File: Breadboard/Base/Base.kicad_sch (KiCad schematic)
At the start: 41 parts, among them J1 Barrel_Jack_Switch, J2 AudioJack2_Ground, J3 AudioJack2_Ground, J4 Conn_01x04_Pin, J5 Conn_01x04_Pin, J6 Conn_Coaxial, J7 Conn_Coaxial, J8 Conn_01x02_Pin, J9 Conn_01x02_Pin, Q1 40V, U1 TLE2426xD, U2 OPA1656

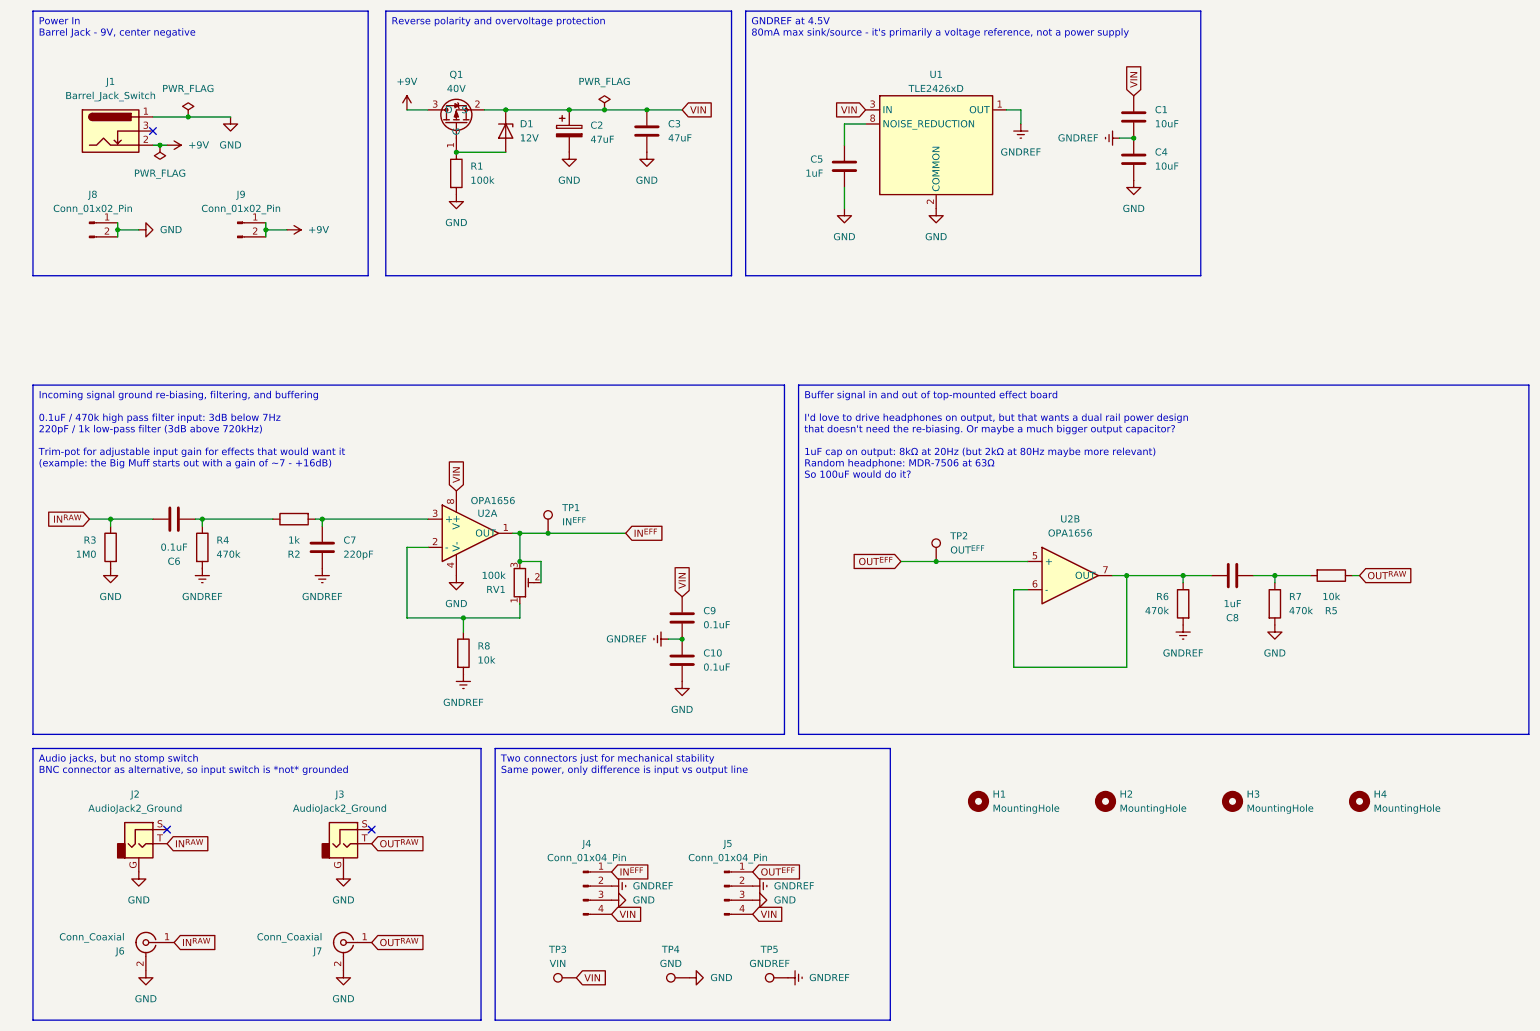
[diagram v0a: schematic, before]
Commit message: Stop trying to pretend that the 4.5V reference voltage is ground
Yes, it was a real ground in the earlier dual rail supply designs, but
in Gen2 that's no longer the case, and the pretense caused issues with
me adding bypass capacitors to that reference voltage rail.

So this just renames it as 'GNDREF' everywhere.  Maybe I should have
called it 'VREF'?

The real ground is still called '-V' in the effects, I'll change that
later too, but let's do this in individual steps.

This also removes the remaining bypass caps to GNDREF, and makes the
ground pours be actual ground.

I also need to come up with something sane for the Rectifier board
potentiometers.

Right now they are bogus random stuff where I am using the pots as
trim-pots for testing, but they don't actually make *sense* (ie the
"Volume" pot isn't actually sane, it ends up being another voltage
divider with the resistors in the low-pass filter trim pot etc).

Signed-off-by: Linus Torvalds <torvalds@linux-foundation.org>
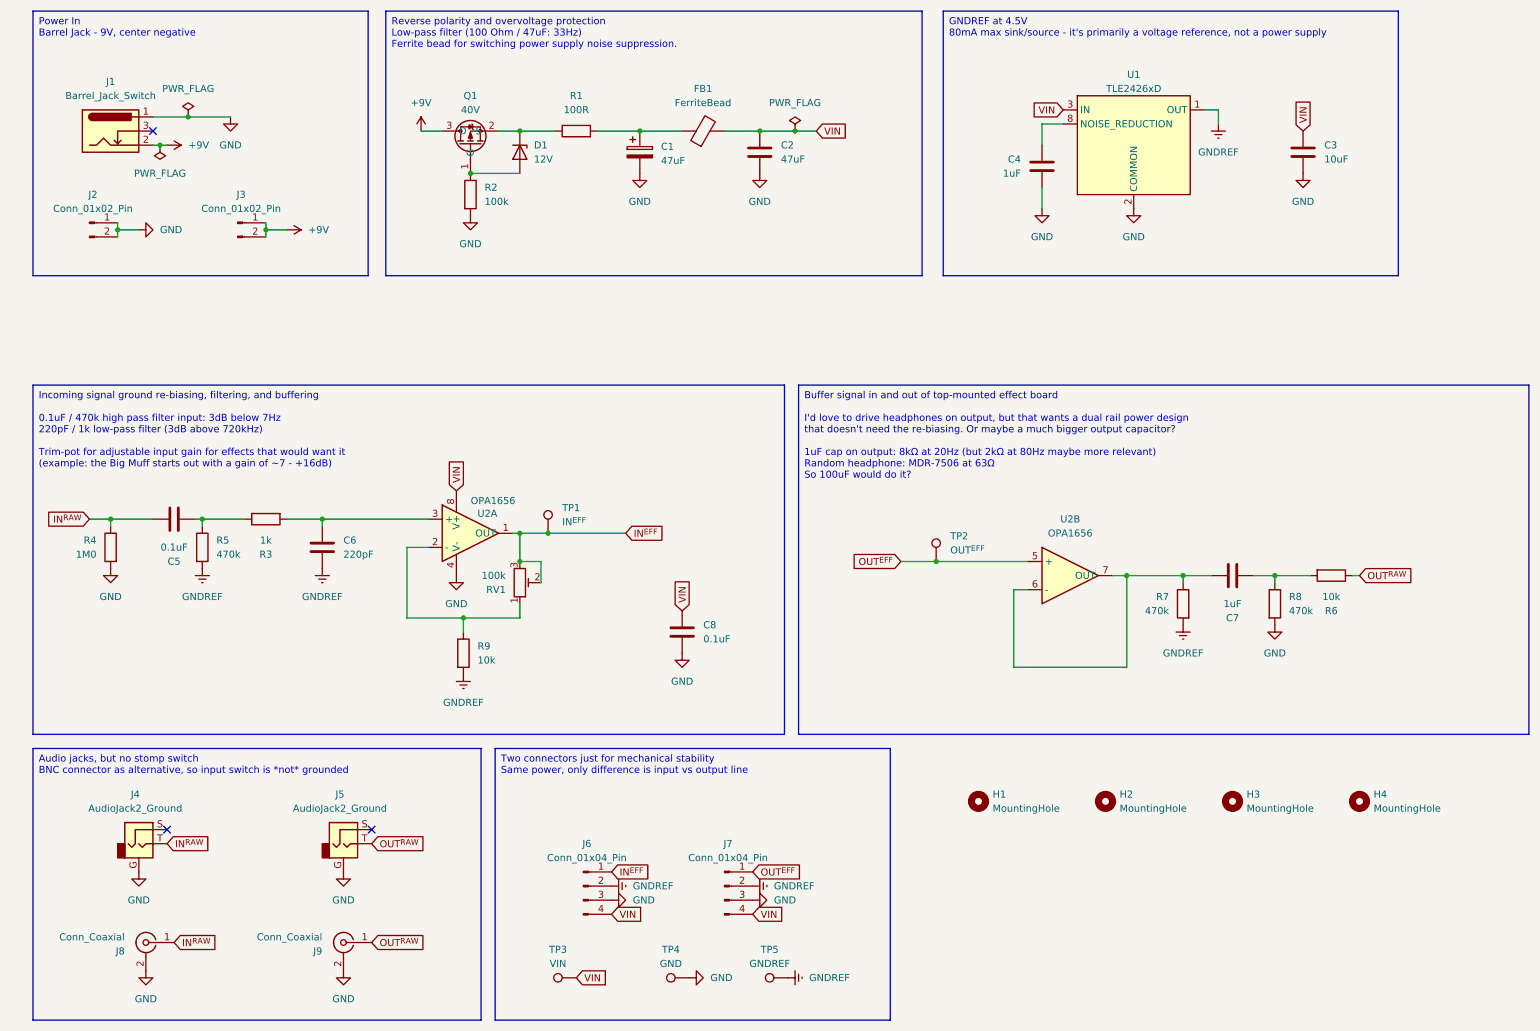
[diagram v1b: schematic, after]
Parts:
- removed C10: 0.1uF, Mylib:C_0704_1810Metric, symbol Device:C
- removed C4: 10uF, Capacitor_SMD:C_1206_3216Metric_Pad1.33x1.80mm_HandSolder, symbol Device:C
- added FB1: FerriteBead, Inductor_SMD:L_1206_3216Metric_Pad1.22x1.90mm_HandSolder, symbol Device:FerriteBead
- added R1: 100R, Resistor_SMD:R_0805_2012Metric_Pad1.20x1.40mm_HandSolder, symbol Device:R
- renumbered C2 to C1, C3 to C2, C1 to C3, C5 to C4, C6 to C5, C7 to C6, C8 to C7, C9 to C8, J8 to J2, J9 to J3, J2 to J4, J3 to J5, J4 to J6, J5 to J7, J6 to J8, J7 to J9, R1 to R2, R2 to R3, R3 to R4, R4 to R5, R5 to R6, R6 to R7, R7 to R8, R8 to R9
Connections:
- net GND: now also C3.2, C8.2
- net GNDREF: no longer C3.2, C8.2
- net VIN: now also FB1.2; no longer C1.1, D1.1 (K), Q1.2 (S)
- new net: C1.1, FB1.1, R1.2
- new net: D1.1 (K), Q1.2 (S), R1.1
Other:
- moved on the sheet: C1, C2, C3, C4, C8, D1, Q1, R2, R3, U1
